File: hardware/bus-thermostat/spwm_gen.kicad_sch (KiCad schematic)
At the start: 18 parts

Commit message: Update some components
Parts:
- added C42: 100nF, symbol Device:C
- added TP10, TP5, TP6, TP9: TestPoint, Connector_Pin:Pin_D0.7mm_L6.5mm_W1.8mm_FlatFork, symbol Connector:TestPoint
- added U22: 74HC2G17GW-Q100H, UltraLibrarian:74HC2G17GW-Q100H, symbol UltraLibrarian:74HC2G17GW-Q100H
- gave numbers to parts that had none: 18
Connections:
- net +6V: now also C42.1, U22.5 (VCC)
- net GND: now also C42.2, U22.2 (GND)
- net SPWM+: now also TP10.1, U22.6 (1Y); no longer TP8.1, U21.3 (-), U21.4
- net SPWM-: now also TP9.1, U22.4 (2Y); no longer TP7.1, U20.3 (-), U20.4
- net at U18.3 (-): now also TP5.1
- new net: TP7.1, U20.3 (-), U20.4, U22.3 (2A)
- new net: TP8.1, U21.3 (-), U21.4, U22.1 (1A)
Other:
- note added: "2 Gate Schmitt Trigger Buffer"
- moved on the sheet: TP7

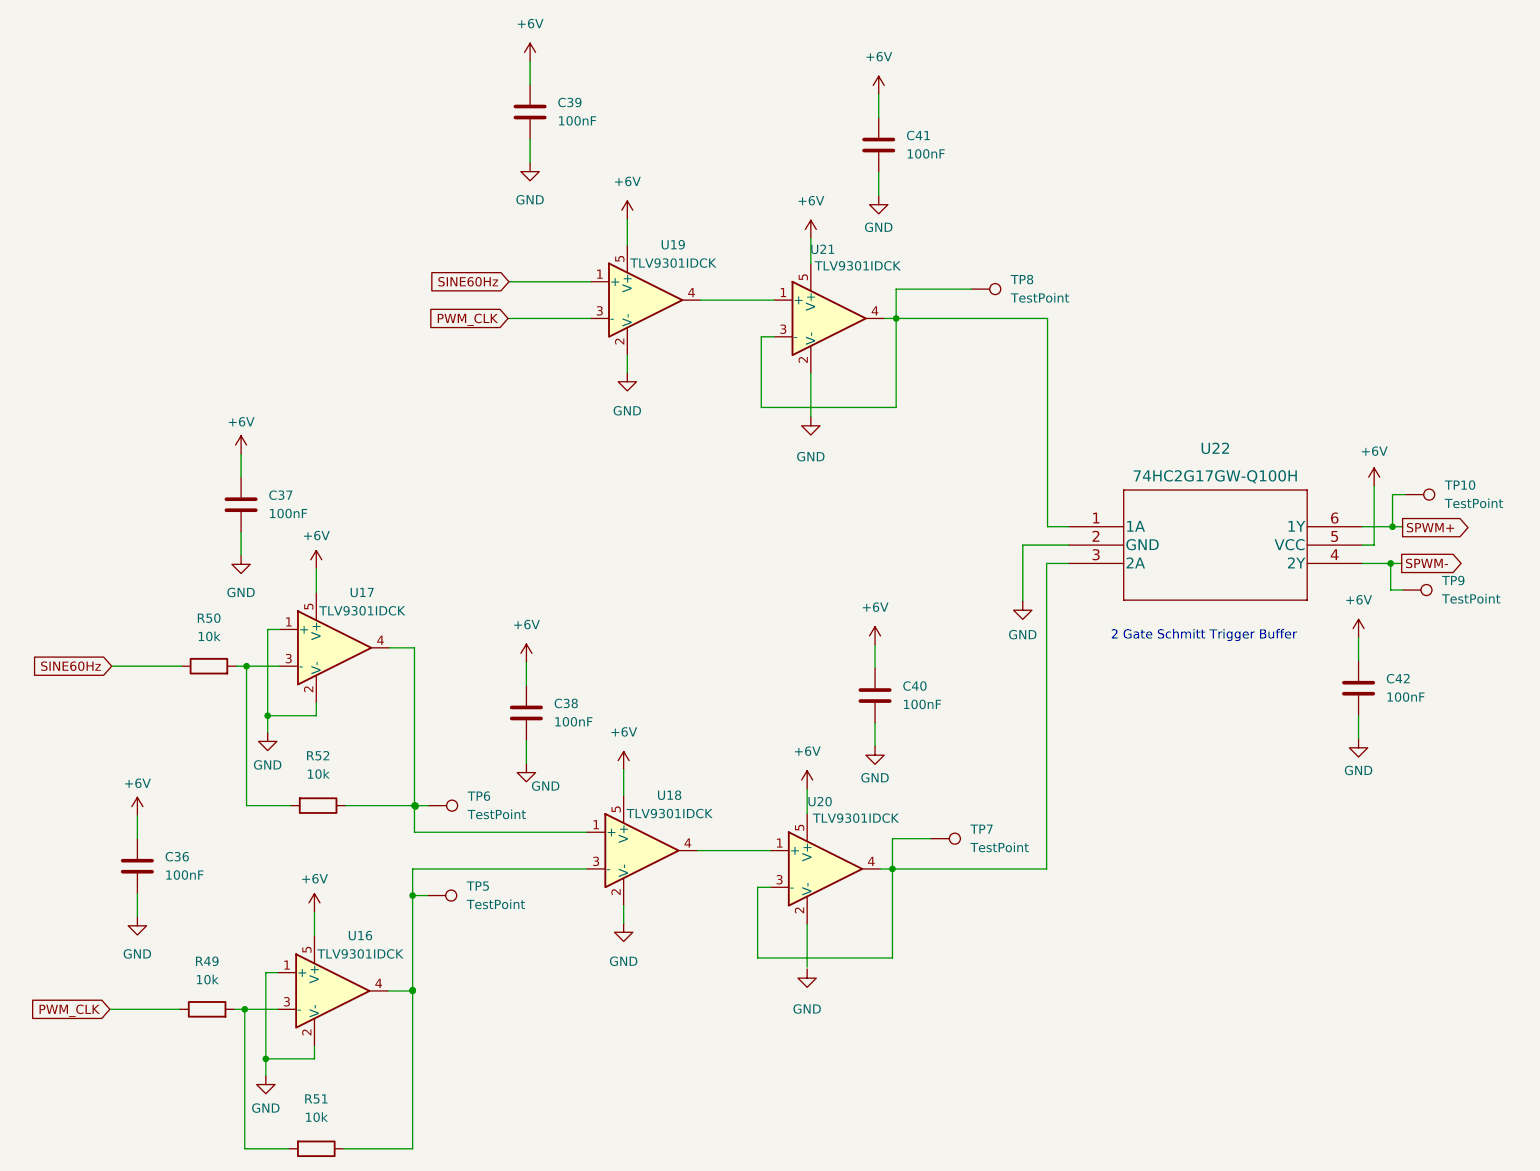
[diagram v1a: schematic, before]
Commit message: Fix oscillator, add fan controller/thermostat and its IOs.
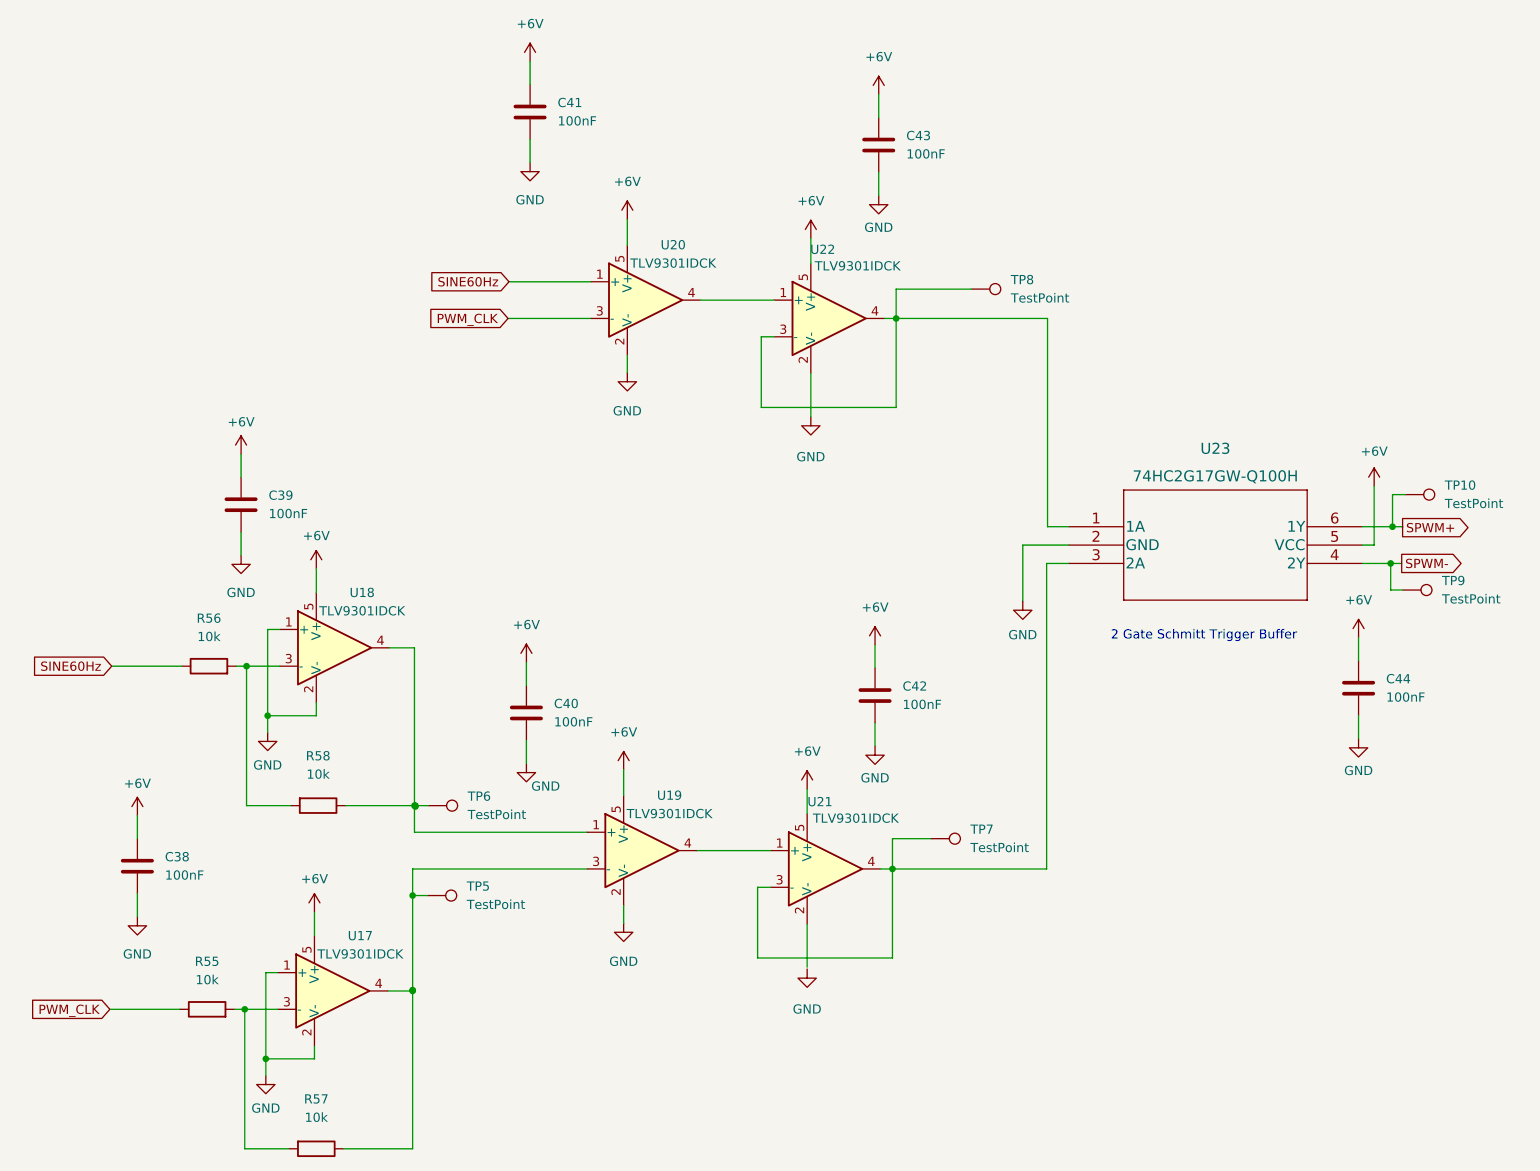
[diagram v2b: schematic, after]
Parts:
- C38: renamed from C36; footprint (none) -> Capacitor_SMD:C_0805_2012Metric_Pad1.18x1.45mm_HandSolder
- C39: renamed from C37; footprint (none) -> Capacitor_SMD:C_0805_2012Metric_Pad1.18x1.45mm_HandSolder
- C40: renamed from C38; footprint (none) -> Capacitor_SMD:C_0805_2012Metric_Pad1.18x1.45mm_HandSolder
- C41: renamed from C39; footprint (none) -> Capacitor_SMD:C_0805_2012Metric_Pad1.18x1.45mm_HandSolder
- C42: renamed from C40; footprint (none) -> Capacitor_SMD:C_0805_2012Metric_Pad1.18x1.45mm_HandSolder
- C43: renamed from C41; footprint (none) -> Capacitor_SMD:C_0805_2012Metric_Pad1.18x1.45mm_HandSolder
- C44: renamed from C42; footprint (none) -> Capacitor_SMD:C_0805_2012Metric_Pad1.18x1.45mm_HandSolder
- R55: renamed from R49; footprint (none) -> Resistor_SMD:R_0805_2012Metric_Pad1.20x1.40mm_HandSolder
- R56: renamed from R50; footprint (none) -> Resistor_SMD:R_0805_2012Metric_Pad1.20x1.40mm_HandSolder
- R57: renamed from R51; footprint (none) -> Resistor_SMD:R_0805_2012Metric_Pad1.20x1.40mm_HandSolder
- R58: renamed from R52; footprint (none) -> Resistor_SMD:R_0805_2012Metric_Pad1.20x1.40mm_HandSolder
- renumbered U16 to U17, U17 to U18, U18 to U19, U19 to U20, U20 to U21, U21 to U22, U22 to U23
